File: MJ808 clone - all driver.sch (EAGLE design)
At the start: 30 parts, among them IC1 MAX16820, IC3 MCP2515, IC4 ATTINY4313-MMH, IC5 MCP2561-2, IC8 PRQV8.00CR1510Y00L, IC9 TPS709-Q1, Q11 PMV213SN,215

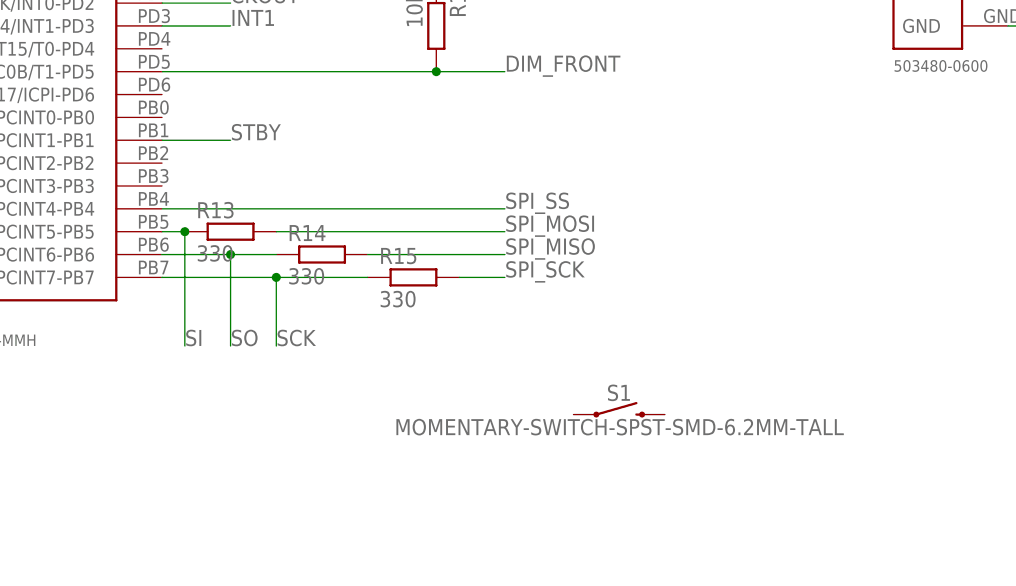
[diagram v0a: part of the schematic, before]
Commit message: - added master switch - unlocked elements on final board
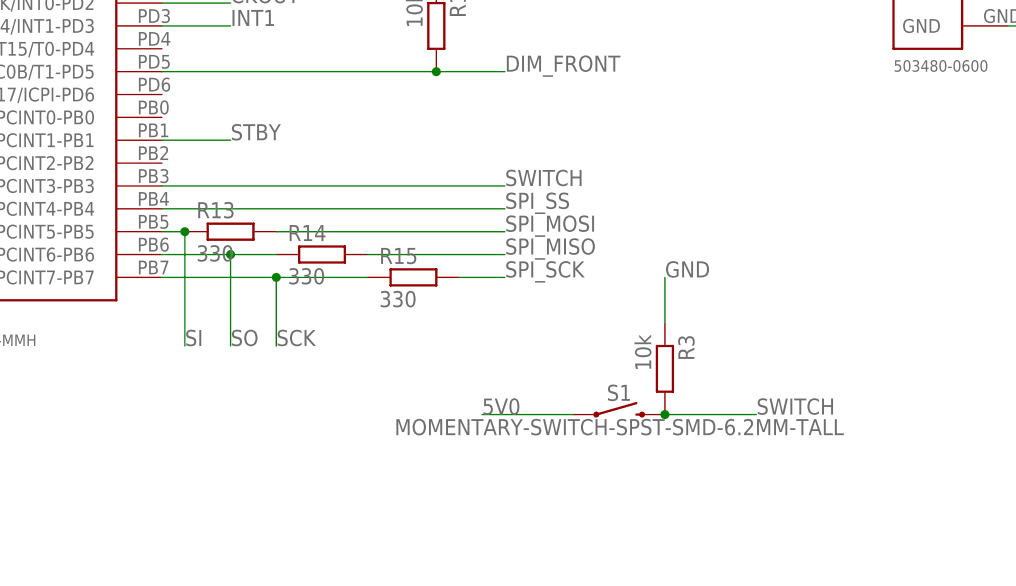
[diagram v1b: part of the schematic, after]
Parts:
- added R3: 10k, rcl:R-EU_R0402
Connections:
- new net SWITCH: IC4.OC1A/PCINT3-PB3, R3.2, S1.2
- net 5V0: now also S1.1
- net GND: now also R3.1
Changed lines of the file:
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@@
 <part name="IC9" library="TPS709-q1 5V LDO" deviceset="TPS709-Q1" device="" value="TPS709-Q1"/>
 <part name="S1" library="SparkFun-Switches" library_urn="urn:adsk.eagle:library:535" deviceset="MOMENTARY-SWITCH-SPST" device="-SMD-6.2MM-TALL" package3d_urn="urn:adsk.eagle:package:40172/1"/>
+<part name="R3" library="rcl" library_urn="urn:adsk.eagle:library:334" deviceset="R-EU_" device="R0402" package3d_urn="urn:adsk.eagle:package:23547/1" value="10k"/>
 </parts>
 <sheets>
@@
 <instance part="IC9" gate="G$1" x="233.68" y="327.66"/>
 <instance part="S1" gate="G$1" x="228.6" y="241.3"/>
+<instance part="R3" gate="G$1" x="233.68" y="246.38" rot="R270"/>
 </instances>
 <busses>
@@
 <label x="210.82" y="325.12" size="1.778" layer="95"/>
 </segment>
+<segment>
+<pinref part="R3" gate="G$1" pin="1"/>
+<wire x1="233.68" y1="251.46" x2="233.68" y2="256.54" width="0.1524" layer="91"/>
+<label x="233.68" y="256.54" size="1.778" layer="95"/>
+</segment>
 </net>
 <net name="DIM_FRONT" class="0">
@@
 <wire x1="325.12" y1="144.78" x2="309.88" y2="144.78" width="0.1524" layer="91"/>
 <junction x="325.12" y="144.78"/>
+</segment>
+<segment>
+<pinref part="S1" gate="G$1" pin="1"/>
+<wire x1="223.52" y1="241.3" x2="213.36" y2="241.3" width="0.1524" layer="91"/>
+<label x="213.36" y="241.3" size="1.778" layer="95"/>
 </segment>
 </net>
@@
 </segment>
 </net>
+<net name="SWITCH" class="0">
+<segment>
+<pinref part="S1" gate="G$1" pin="2"/>
+<wire x1="233.68" y1="241.3" x2="243.84" y2="241.3" width="0.1524" layer="91"/>
+<pinref part="R3" gate="G$1" pin="2"/>
+<junction x="233.68" y="241.3"/>
+<label x="243.84" y="241.3" size="1.778" layer="95"/>
+</segment>
+<segment>
+<pinref part="IC4" gate="G$1" pin="OC1A/PCINT3-PB3"/>
+<wire x1="177.8" y1="266.7" x2="215.9" y2="266.7" width="0.1524" layer="91"/>
+<label x="215.9" y="266.7" size="1.778" layer="95"/>
+</segment>
+</net>

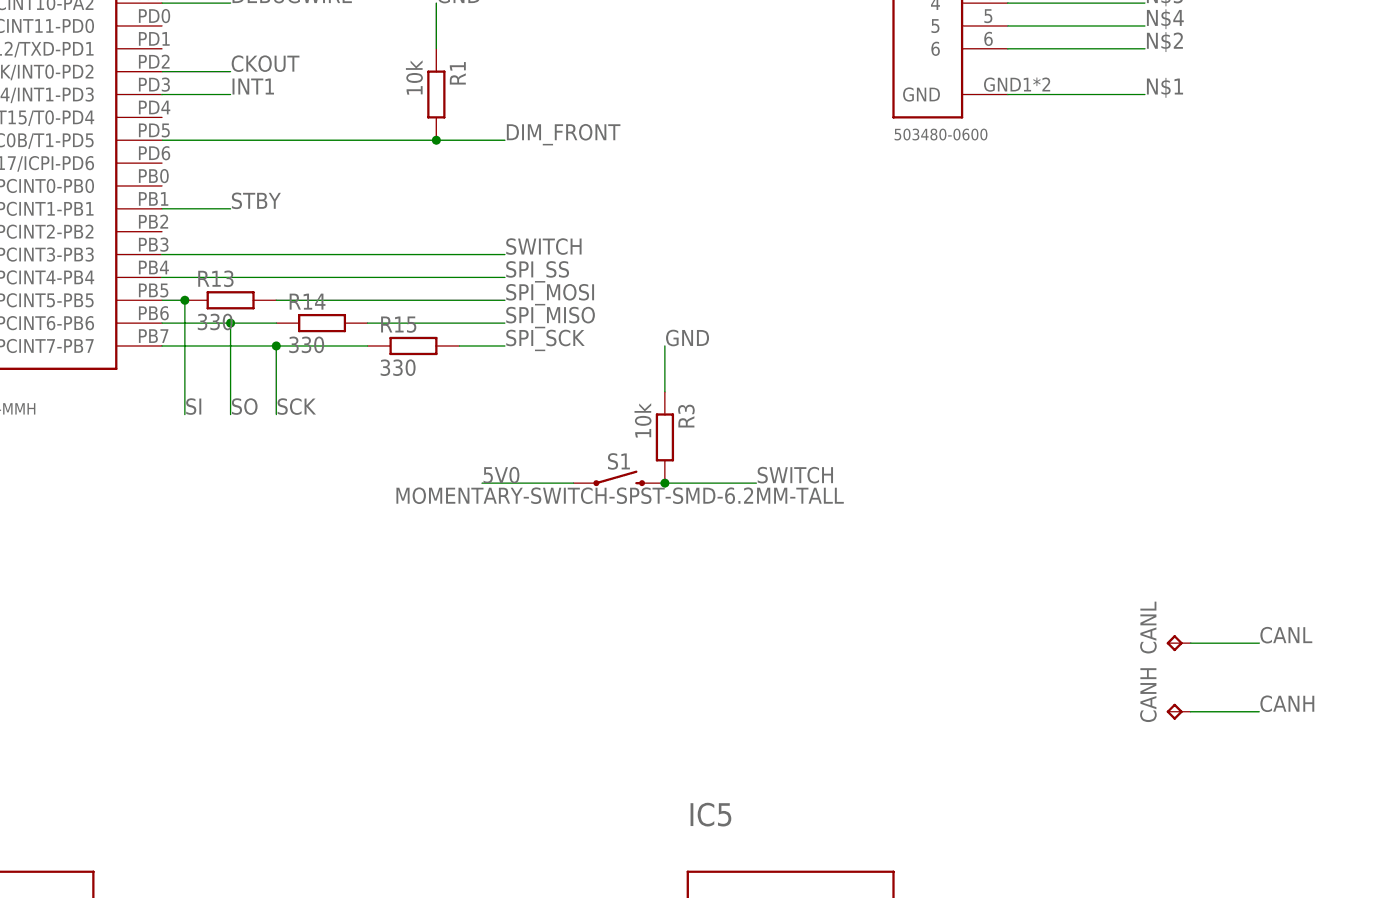
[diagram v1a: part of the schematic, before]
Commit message: - updated CAM job, redo of gerbers
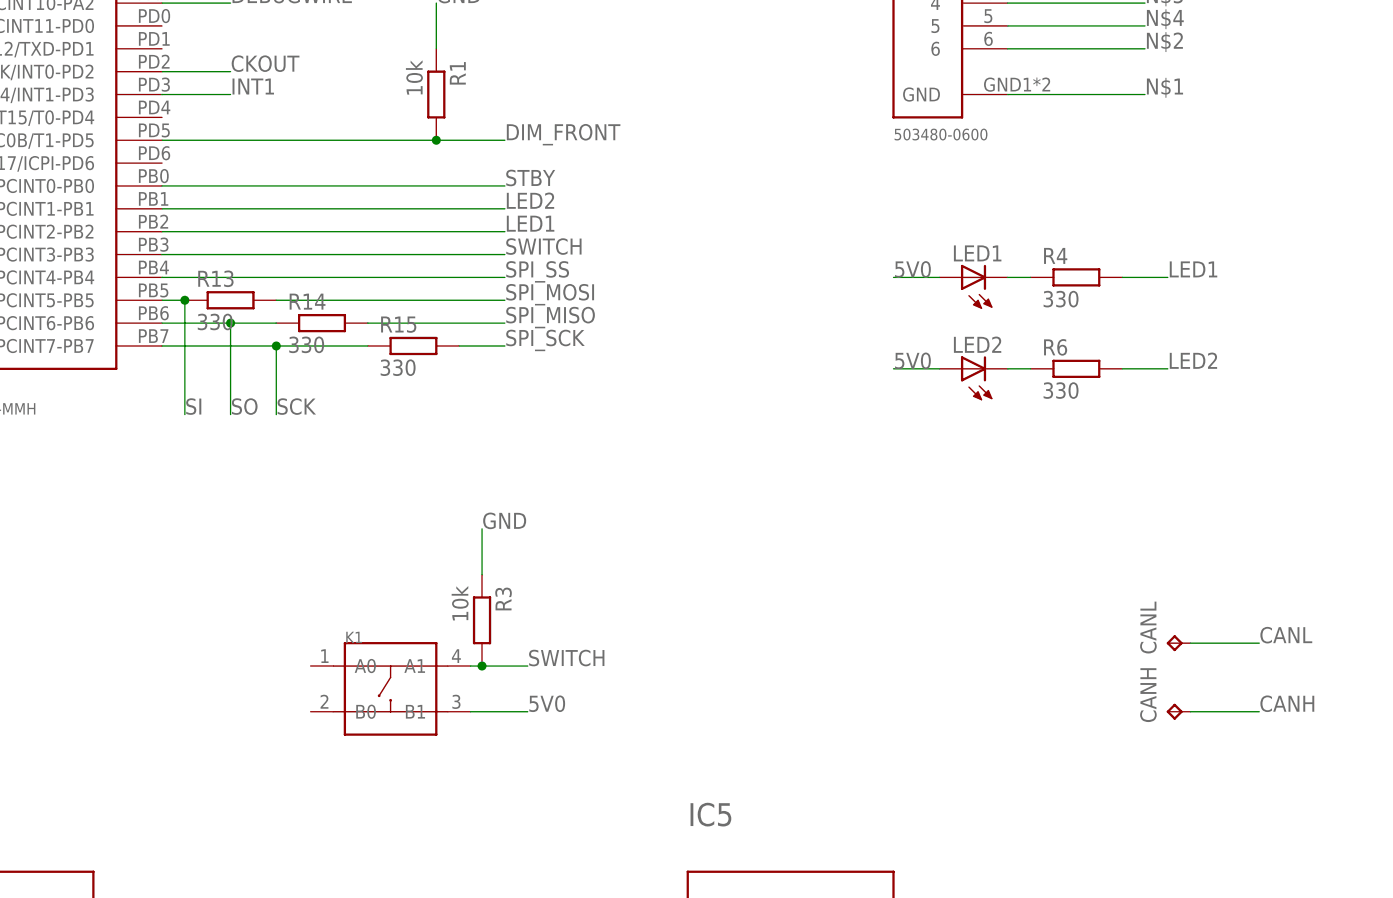
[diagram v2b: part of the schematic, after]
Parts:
- removed S1: MOMENTARY-SWITCH-SPST-SMD-6.2MM-TALL, SparkFun-Switches:MOMENTARY-SWITCH-SPST-SMD-6.2MM-TALL
- added K1: (no value), Seeed-Switch:SMD-SWITCH-TACTILE-SPST-NO(4P-D6.0MM)
- added LED1, LED2: (no value), led:LEDCHIP-LED0805
- added R4, R6: 330, rcl:R-EU_R0402
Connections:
- new net LED1: IC4.OC0A/PCINT2-PB2, R4.2
- new net LED2: IC4.AIN1/PCINT1-PB1, R6.2
- new net N$11: LED2.C, R6.1
- new net N$12: LED1.C, R4.1
- net 5V0: now also K1.B1, LED1.A, LED2.A; no longer S1.1
- net STBY: now also IC4.AIN0/PCINT0-PB0; no longer IC4.AIN1/PCINT1-PB1
- net SWITCH: now also K1.A1; no longer S1.2
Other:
- moved on the sheet: R3
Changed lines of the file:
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@@
 <part name="R15" library="rcl" library_urn="urn:adsk.eagle:library:334" deviceset="R-EU_" device="R0402" package3d_urn="urn:adsk.eagle:package:23547/1" value="330"/>
 <part name="IC9" library="TPS709-q1 5V LDO" deviceset="TPS709-Q1" device="" value="TPS709-Q1"/>
-<part name="S1" library="SparkFun-Switches" library_urn="urn:adsk.eagle:library:535" deviceset="MOMENTARY-SWITCH-SPST" device="-SMD-6.2MM-TALL" package3d_urn="urn:adsk.eagle:package:40172/1"/>
 <part name="R3" library="rcl" library_urn="urn:adsk.eagle:library:334" deviceset="R-EU_" device="R0402" package3d_urn="urn:adsk.eagle:package:23547/1" value="10k"/>
+<part name="LED1" library="led" library_urn="urn:adsk.eagle:library:259" deviceset="LED" device="CHIP-LED0805" package3d_urn="urn:adsk.eagle:package:15818/1"/>
+<part name="LED2" library="led" library_urn="urn:adsk.eagle:library:259" deviceset="LED" device="CHIP-LED0805" package3d_urn="urn:adsk.eagle:package:15818/1"/>
+<part name="R4" library="rcl" library_urn="urn:adsk.eagle:library:334" deviceset="R-EU_" device="R0402" package3d_urn="urn:adsk.eagle:package:23547/1" value="330"/>
+<part name="R6" library="rcl" library_urn="urn:adsk.eagle:library:334" deviceset="R-EU_" device="R0402" package3d_urn="urn:adsk.eagle:package:23547/1" value="330"/>
+<part name="K1" library="Seeed-Switch" library_urn="urn:adsk.eagle:library:476" deviceset="SMD-SWITCH-TACTILE-SPST-NO(4P-D6.0MM)" device="" package3d_urn="urn:adsk.eagle:package:32987/1"/>
 </parts>
 <sheets>
@@
 <instance part="R15" gate="G$1" x="205.74" y="256.54"/>
 <instance part="IC9" gate="G$1" x="233.68" y="327.66"/>
-<instance part="S1" gate="G$1" x="228.6" y="241.3"/>
-<instance part="R3" gate="G$1" x="233.68" y="246.38" rot="R270"/>
+<instance part="R3" gate="G$1" x="213.36" y="226.06" rot="R270"/>
+<instance part="LED1" gate="G$1" x="266.7" y="264.16" rot="R90"/>
+<instance part="LED2" gate="G$1" x="266.7" y="254" rot="R90"/>
+<instance part="R4" gate="G$1" x="279.4" y="264.16"/>
+<instance part="R6" gate="G$1" x="279.4" y="254"/>
+<instance part="K1" gate="G$1" x="203.2" y="218.44"/>
 </instances>
 <busses>
@@
 <segment>
 <pinref part="R3" gate="G$1" pin="1"/>
-<wire x1="233.68" y1="251.46" x2="233.68" y2="256.54" width="0.1524" layer="91"/>
-<label x="233.68" y="256.54" size="1.778" layer="95"/>
+<wire x1="213.36" y1="231.14" x2="213.36" y2="236.22" width="0.1524" layer="91"/>
+<label x="213.36" y="236.22" size="1.778" layer="95"/>
 </segment>
 </net>
@@
 </segment>
 <segment>
-<pinref part="S1" gate="G$1" pin="1"/>
-<wire x1="223.52" y1="241.3" x2="213.36" y2="241.3" width="0.1524" layer="91"/>
-<label x="213.36" y="241.3" size="1.778" layer="95"/>
+<pinref part="LED1" gate="G$1" pin="A"/>
+<wire x1="264.16" y1="264.16" x2="259.08" y2="264.16" width="0.1524" layer="91"/>
+<label x="259.08" y="264.16" size="1.778" layer="95"/>
+</segment>
+<segment>
+<pinref part="LED2" gate="G$1" pin="A"/>
+<wire x1="264.16" y1="254" x2="259.08" y2="254" width="0.1524" layer="91"/>
+<label x="259.08" y="254" size="1.778" layer="95"/>
+</segment>
+<segment>
+<pinref part="K1" gate="G$1" pin="B1"/>
+<wire x1="212.09" y1="215.9" x2="218.44" y2="215.9" width="0.1524" layer="91"/>
+<label x="218.44" y="215.9" size="1.778" layer="95"/>
 </segment>
 </net>
@@
 </segment>
 <segment>
-<pinref part="IC4" gate="G$1" pin="AIN1/PCINT1-PB1"/>
-<wire x1="177.8" y1="271.78" x2="185.42" y2="271.78" width="0.1524" layer="91"/>
-<label x="185.42" y="271.78" size="1.778" layer="95"/>
+<pinref part="IC4" gate="G$1" pin="AIN0/PCINT0-PB0"/>
+<wire x1="177.8" y1="274.32" x2="215.9" y2="274.32" width="0.1524" layer="91"/>
+<label x="215.9" y="274.32" size="1.778" layer="95"/>
 </segment>
 </net>
@@
 <net name="SWITCH" class="0">
 <segment>
-<pinref part="S1" gate="G$1" pin="2"/>
-<wire x1="233.68" y1="241.3" x2="243.84" y2="241.3" width="0.1524" layer="91"/>
+<wire x1="213.36" y1="220.98" x2="218.44" y2="220.98" width="0.1524" layer="91"/>
 <pinref part="R3" gate="G$1" pin="2"/>
-<junction x="233.68" y="241.3"/>
-<label x="243.84" y="241.3" size="1.778" layer="95"/>
+<label x="218.44" y="220.98" size="1.778" layer="95"/>
+<pinref part="K1" gate="G$1" pin="A1"/>
+<wire x1="212.09" y1="220.98" x2="213.36" y2="220.98" width="0.1524" layer="91"/>
+<junction x="213.36" y="220.98"/>
 </segment>
 <segment>
@@
 </segment>
 </net>
+<net name="N$11" class="0">
+<segment>
+<pinref part="R6" gate="G$1" pin="1"/>
+<pinref part="LED2" gate="G$1" pin="C"/>
+<wire x1="274.32" y1="254" x2="271.78" y2="254" width="0.1524" layer="91"/>
+</segment>
+</net>
+<net name="N$12" class="0">
+<segment>
+<pinref part="LED1" gate="G$1" pin="C"/>
+<pinref part="R4" gate="G$1" pin="1"/>
+<wire x1="271.78" y1="264.16" x2="274.32" y2="264.16" width="0.1524" layer="91"/>
+</segment>
+</net>
+<net name="LED1" class="0">
+<segment>
+<pinref part="R4" gate="G$1" pin="2"/>
+<wire x1="284.48" y1="264.16" x2="289.56" y2="264.16" width="0.1524" layer="91"/>
+<label x="289.56" y="264.16" size="1.778" layer="95"/>
+</segment>
+<segment>
+<pinref part="IC4" gate="G$1" pin="OC0A/PCINT2-PB2"/>
+<wire x1="177.8" y1="269.24" x2="215.9" y2="269.24" width="0.1524" layer="91"/>
+<label x="215.9" y="269.24" size="1.778" layer="95"/>
+</segment>
+</net>
+<net name="LED2" class="0">
+<segment>
+<pinref part="R6" gate="G$1" pin="2"/>
+<wire x1="284.48" y1="254" x2="289.56" y2="254" width="0.1524" layer="91"/>
+<label x="289.56" y="254" size="1.778" layer="95"/>
+</segment>
+<segment>
+<pinref part="IC4" gate="G$1" pin="AIN1/PCINT1-PB1"/>
+<wire x1="177.8" y1="271.78" x2="215.9" y2="271.78" width="0.1524" layer="91"/>
+<label x="215.9" y="271.78" size="1.778" layer="95"/>
+</segment>
+</net>

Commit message: - redraw of POC board according to 1st rev of prod board, ERC & DRC check out error free, updated gerbers
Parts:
- removed C3: 0.1μF, rcl:C-EUC0402
- removed C8: 1μF, rcl:C-EUC0402
- removed IC8: PRQV8.00CR1510Y00L, PRQV8.00CR1510Y00L - 8MHz resonator:PRQV
- removed IC9: TPS709-Q1, TPS709-q1 5V LDO:TPS709-Q1
- removed K1: (no value), Seeed-Switch:SMD-SWITCH-TACTILE-SPST-NO(4P-D6.0MM)
- removed LED2: (no value), led:LEDCHIP-LED0805
- removed PROG: 503480-0600, 5034800600 FPC Connector:5034800600
- removed Q11: PMV213SN,215, adafruit:MOSFET-NREFLOW
- removed R13, R14, R15: 330, rcl:R-EU_R0402
- removed VBAT: TPTP20R, testpad:TPTP20R
- added BAT+: LiIon + Terminal, signal testpoint:TP
- added C2: 22μF, rcl:C-EUC0603
- added IC2: PRQV8.00CR1510Y00L, PRQV8.00CR1510Y00L - 8MHz resonator:PRQV
- added IC6: MCP2561-2, MCP2561-2 - High-Speed CAN Transceiver:MCP2561-2
- added IC7: MAX16820, MAX16820 LED Driver, constant current:MAX16820
- added ICSP: 5034800600, 5034800600 FPC Connector:5034800600
- added Q1: PMV213SN,215, adafruit:MOSFET-NREFLOW
- added R10: 0.15 / 1W, rcl:R-EU_R1210
- added R11, R9: 10k, rcl:R-EU_R0402
- added R12: 120, rcl:R-EU_R0805
- added SW1: TL3305-844809, TL3305-844809 SPST-NO Tact Switch:TL3305-844809
- C1: value 47μF / 15V+ -> 0.1μF; device rcl:C-EUC0805 -> rcl:C-EUC0402
- C4: value 0.1μF -> 47μF / 15V+; device rcl:C-EUC0402 -> rcl:C-EUC0805
- C5: value 0.1μF -> 22μF; device rcl:C-EUC0402 -> rcl:C-EUC0603
- CANH: value TPTP20R -> CAN high; device testpad:TPTP20R -> signal testpoint:TP
- CANL: value TPTP20R -> CAN low; device testpad:TPTP20R -> signal testpoint:TP
- GND: value TPTP20R -> LiIon - Terminal; device testpad:TPTP20R -> signal testpoint:TP
- IC1: value MAX16820 -> ATTINY4313-MMH; device MAX16820 LED Driver, constant current:MAX16820 -> ATtiny4313 microcontroller:ATTINY4313VQFN-20; SPICEPREFIX (none) -> X
- IC3: value MCP2515 -> LP38693SD-5.0/NOPB; device MCP2515-I-ML - Standalonce CAN Controller with SPI Interface:MCP2515-I-ML -> LP38693 5V LDO:LP38693
- IC4: value ATTINY4313-MMH -> LP38693SD-5.0/NOPB; device ATtiny4313 microcontroller:ATTINY4313VQFN-20 -> LP38693 5V LDO:LP38693
- IC5: value MCP2561-2 -> MCP2515; device MCP2561-2 - High-Speed CAN Transceiver:MCP2561-2 -> MCP2515-I-ML - Standalonce CAN Controller with SPI Interface:MCP2515-I-ML
- L1: value AISC-1210HS-330K-T2 -> VLS6045EX-150M-CA; device eagle-ltspice:LL3225M -> SparkFun-Coils:INDUCTOR-SRN6045-33UH
- LED+: value TPTP20R -> LED anode; device testpad:TPTP20R -> signal testpoint:TP
- LED-: value TPTP20R -> LED cathode; device testpad:TPTP20R -> signal testpoint:TP
- LED1: value (none) -> APHBM2012LSURKZGKC; device led:LEDCHIP-LED0805 -> APHBM2012LSURKZGKC:APHBM2012LSURKZGKC
- R2: value 0.25 / 0.25W -> 10k; device rcl:R-EU_R1206 -> rcl:R-EU_R0402
- R5: value 120 -> 330; device rcl:R-EU_R0805 -> rcl:R-EU_R0402
- R6: value 330 -> 10k
- R7: value 10k -> 330
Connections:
- removed net 5V0: C4.1, C8.1, IC1.VCC, IC4.VCC, K1.B1, LED1.A, LED2.A
- removed net 5V0_REG: C3.1, C5.1, IC3.VDD, IC5.VCC, IC9.OUT, R8.1
- removed net CKOUT: IC3.OSC1, IC4.PCINT13/CKOUT/XCK/INT0-PD2
- removed net CSN: IC1.CS, LED+.TP, R2.1
- removed net DEBUGWIRE: IC4.!RESET!/DW/PCINT10-PA2
- removed net INT1: IC3.!INT!, IC4.PCINT14/INT1-PD3
- removed net LED1: IC4.OC0A/PCINT2-PB2, R4.2
- removed net LED2: IC4.AIN1/PCINT1-PB1, R6.2
- removed net N$1: PROG.GND
- removed net N$11: LED2.C, R6.1
- removed net N$12: LED1.C, R4.1
- removed net N$2: PROG.6
- removed net N$3: L1.2, LED-.TP
- removed net N$4: PROG.5
- removed net N$5: PROG.4
- removed net N$6: PROG.3
- removed net N$7: PROG.2
- removed net N$8: PROG.1
- removed net SCK: IC4.USCK/SCL/SCK/PCINT7-PB7, R15.1
- removed net SI: IC4.MOSI/DI/SDA/PCINT5-PB5, R13.1
- removed net SO: IC4.MISO/DO/PCINT6-PB6, R14.1
- removed net VBAT: C1.1, D1.C, IC1.IN, IC9.IN, R2.2, VBAT.TP
- new net 5V0_CAN: C2.1, IC3.OUT, IC3.SNS, IC5.VDD, IC6.VCC, R11.1, R6.1
- new net 5V0_μC: C1.1, C5.2, IC1.VCC, IC4.OUT, ICSP.5, R2.2, SW1.P$1
- new net BAT+: BAT+.TP$1, C4.1, D1.C, IC3.IN, IC4.EN, IC4.IN, IC7.IN, R10.2
- new net CLOCKOUT: IC1.PCINT13/CKOUT/XCK/INT0-PD2, IC5.OSC1
- new net DEBUGWIRE/RESET: IC1.!RESET!/DW/PCINT10-PA2, ICSP.6
- new net GREEN_LED: IC1.RXD/PCINT11-PD0, LED1.3
- new net ICSP_MISO: IC1.MISO/DO/PCINT6-PB6, ICSP.3, R7.2
- new net ICSP_MOSI: IC1.MOSI/DI/SDA/PCINT5-PB5, ICSP.2, R5.2
- new net ICSP_SCK: IC1.USCK/SCL/SCK/PCINT7-PB7, ICSP.4, R4.2
- new net INT: IC1.PCINT14/INT1-PD3, IC5.!INT!
- new net LED: LED1.1, LED1.4, R2.1
- new net LED_AN: IC7.CS, LED+.TP$1, R10.1
- new net LED_CA: L1.2, LED-.TP$1
- new net RED_LED: IC1.PCINT12/TXD-PD1, LED1.2
- net CANH: now also CANH.TP$1, IC6.CANH, R12.2; no longer CANH.TP, IC5.CANH, R5.2
- net CANL: now also CANL.TP$1, IC6.CANL, R12.1; no longer CANL.TP, IC5.CANL, R5.1
- net DIM_BRAKE_DRAIN: now also Q1.D; no longer Q11.D
- net DIM_FRONT: now also IC1.PCINT16/OC0B/T1-PD5, IC7.DIM, R9.1; no longer IC1.DIM, IC4.PCINT16/OC0B/T1-PD5, R1.2
- net DIM_FRONT_GATE: now also IC7.DRV, R8.1; no longer IC1.DRV, R7.1
- net EN: now also IC1.OC1A/PCINT3-PB3, IC3.EN, R3.2; no longer IC9.EN
- net GATE: now also Q1.G, R8.2; no longer Q11.G, R7.2
- net GND: now also C2.2, C5.1, GND.TP$1, IC2.GND, IC6.GND, IC7.GND, ICSP.1, ICSP.GND, Q1.S, R1.2, R9.2; no longer C3.2, C5.2, C8.2, GND.TP, IC8.GND, IC9.GND, Q11.S, R1.1
- net RXCAN: now also IC5.RXCAN, IC6.RXD; no longer IC3.RXCAN, IC5.RXD
- net SPI_MISO: now also IC5.SO, R7.1; no longer IC3.SO, R14.2
- net SPI_MOSI: now also IC5.SI, R5.1; no longer IC3.SI, R13.2
- net SPI_SCK: now also IC5.SCK, R4.1; no longer IC3.SCK, R15.2
- net SPI_SS: now also IC1.OC1B/PCINT4-PB4, IC5.!CS!, R6.2; no longer IC3.!CS!, IC4.OC1B/PCINT4-PB4, R8.2
- net STBY: now also IC1.OC0A/PCINT2-PB2, IC6.STBY, R11.2; no longer IC4.AIN0/PCINT0-PB0, IC5.STBY
- net SWITCH: now also IC1.PCINT15/T0-PD4, R1.1, SW1.P$2; no longer IC4.OC1A/PCINT3-PB3, K1.A1, R3.2
- net TXCAN: now also IC5.TXCAN, IC6.TXD; no longer IC3.TXCAN, IC5.TXD
- net XTAL1: now also IC1.PCINT8/CLKI/XTAL1-PA0, IC2.XTAL1; no longer IC4.PCINT8/CLKI/XTAL1-PA0, IC8.XTAL1
- net XTAL2: now also IC1.PCINT9/XTAL2-PA1, IC2.XTAL2; no longer IC4.PCINT9/XTAL2-PA1, IC8.XTAL2
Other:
- note added: "CAN bus"
- note added: "CAN infrastructure"
- note added: "ICSP connector"
- note added: "Liion battery - 2S"
- note added: "power supply for CAN infrastructure"
- note added: "power supply for microcontroller"
- note added: "tactile pushbutton"
- note added: "white LED Cree XMLBWT-00-0000-0000U20E2"
- note added: "white LED driver"
- moved on the sheet: C1, C4, C5, D1, R1, R2, R3, R4, R5, R6, R7, R8
